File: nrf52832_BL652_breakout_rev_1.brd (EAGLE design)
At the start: 38.8 x 25.5 mm, 23 parts, among them IC1 E73_2G4M04S

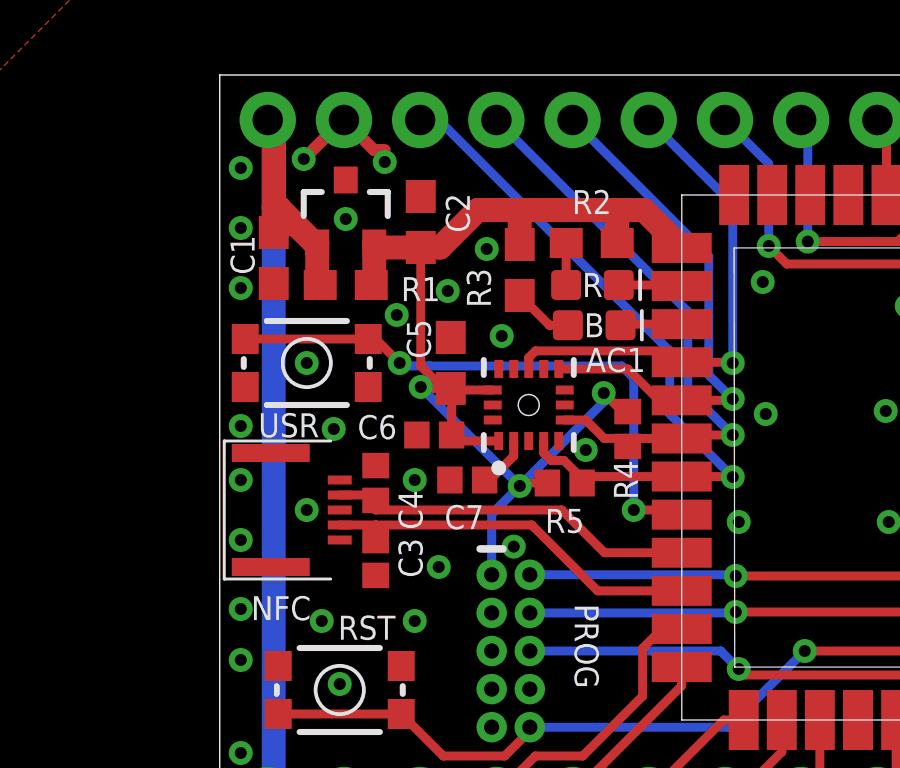
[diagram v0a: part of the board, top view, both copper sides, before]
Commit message: added project for laird nrf52832 module and holyiot nrf52840 module
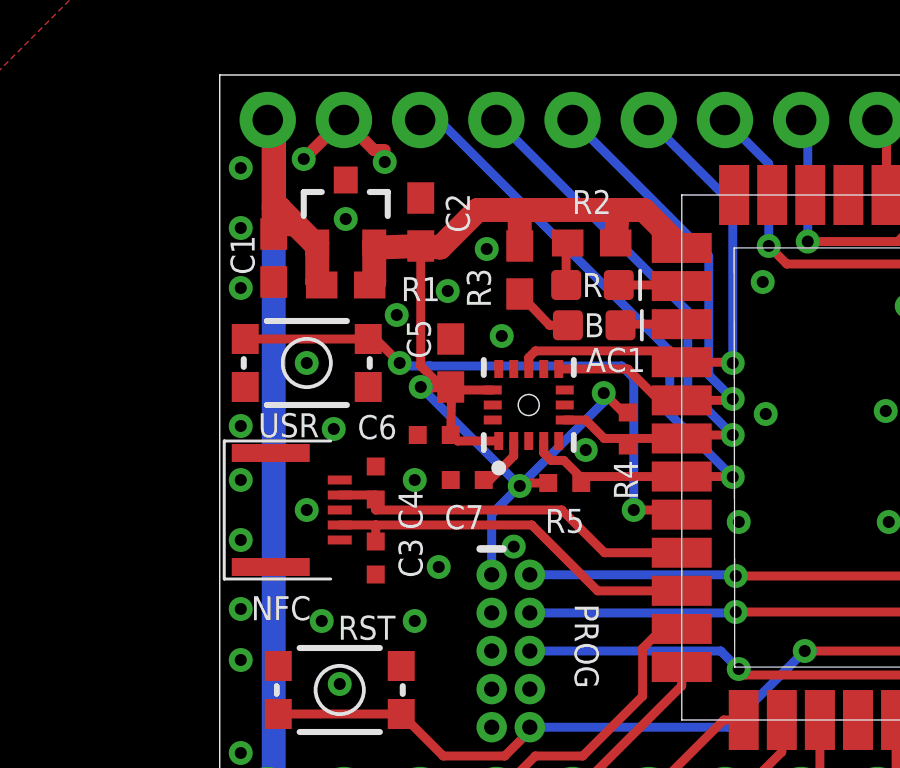
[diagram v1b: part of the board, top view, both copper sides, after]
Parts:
- AC1: device BauckLib:PQFN50P300X300X100-16N -> Inventas-IC:PQFN50P300X300X100-16N
- C1, C2, C5: device SparkFun-Capacitors:0603 -> Inventas-Passives:C0603
- C3, C4, C6, C7: device SparkFun-Capacitors:0402 -> Inventas-Passives:C0402
- D1, D2: device SparkFun-LED:LED-0603 -> inventas_LEDs:LED-0603
- IC1: device BauckLib:E73_2G4M04S -> Inventas-IC:E73_2G4M04S
- J1, J2: value (none) -> NO_BOM
- NFC: device BauckLib:51281-0594 -> Inventas-Connectors:51281-0594
- PROG: device SparkFun-Connectors:2X5-PTH-1.27MM -> Inventas-Connectors:2X5-PTH-1.27MM
- R1: value 0R -> DNM; device SparkFun-Resistors:0603 -> Inventas-Passives:R0603
- R2, R3: device SparkFun-Resistors:0603 -> Inventas-Passives:R0603
- R4, R5: device SparkFun-Resistors:0402 -> Inventas-Passives:R0402
- RST, USR: value (none) -> KMR2; device SparkFun-Switches:TACTILE_SWITCH_SMD_4.6X2.8MM -> Inventas-Buttons:TACTILE_SWITCH_SMD_4.6X2.8MM
- U$1: device BauckLib:SOT23-3 -> Inventas-Power:SOT23-3
- turned D1 to 180 degrees
- turned D2 to 180 degrees
